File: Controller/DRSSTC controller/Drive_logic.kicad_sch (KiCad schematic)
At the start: 70 parts, among them J501 Conn_01x01_Female, J502 Screw_Terminal_01x02, J503 Conn_01x01_Female, J504 Conn_01x01_Female, J505 Screw_Terminal_01x02, J506 Conn_01x01_Female, J507 Conn_01x03_Male, J508 Conn_01x02_Male, J509 Conn_01x02_Male, J510 Conn_01x02_Male, U501 Optical_reciver, U502 Optical_reciver, U503 74HC14, U504 LM311, U505 74HC74, U506 74LS00, U507 TLV7031DBV

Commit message: 0.1V control-circuit
Next relese:
Mounting holes;
Fan header;
Better layout;
Bigger  capacitors;
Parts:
- removed J501, J503, J504, J506: Conn_01x01_Female, Connector_PinHeader_2.54mm:PinHeader_1x01_P2.54mm_Vertical, symbol Connector:Conn_01x01_Female
- removed J502, J505: Screw_Terminal_01x02, TerminalBlock:TerminalBlock_Altech_AK300-2_P5.00mm, symbol Connector:Screw_Terminal_01x02
- added J1, J3, J4, J6: Conn_01x01_Female, Connector_PinHeader_2.54mm:PinHeader_1x01_P2.54mm_Vertical, symbol Connector:Conn_01x01_Female
- added J2, J5: Screw_Terminal_01x02, TerminalBlock_Phoenix:TerminalBlock_Phoenix_PT-1,5-2-3.5-H_1x02_P3.50mm_Horizontal, symbol Connector:Screw_Terminal_01x02
- C513: footprint Capacitor_SMD:C_01005_0402Metric -> Capacitor_SMD:C_0805_2012Metric
- D509, D510: footprint (none) -> LED_SMD:LED_0805_2012Metric
- R503: footprint Resistor_SMD:R_0805_2012Metric -> Resistor_SMD:R_2010_5025Metric
- R506: footprint Resistor_SMD:R_1206_3216Metric -> Resistor_SMD:R_2010_5025Metric
- R515, R516: footprint (none) -> Resistor_SMD:R_0805_2012Metric
- RV501: value 19k -> 10k
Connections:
- net at C509.2, R505.2: now also J5.1 (Pin_1), J6.1 (Pin_1)
- net at C509.1, C511.1, J507.2 (Pin_2)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: now also J4.1 (Pin_1), J5.2 (Pin_2)
- net at D503.2 (A), D504.1 (K): now also J2.1 (Pin_1), J3.1 (Pin_1)
- net at D501.2 (A), D502.1 (K): now also J1.1 (Pin_1), J2.2 (Pin_2)

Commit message: V0.2a
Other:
- company: (none) -> Politehnika
- title: (none) -> DRSSTC controller
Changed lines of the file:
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@@
 (kicad_sch (version 20211123) (generator eeschema)
   (paper "A4")
+  (title_block
+    (title "DRSSTC controller")
+    (date "2023-03-07")
+    (rev "0.2")
+    (company "Politehnika")
+  )
   (junction (at 73.025 24.765) (diameter 0) (color 0 0 0 0)
   )

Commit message: V0.2c
Added stl files
PCB update
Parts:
- renumbered C501 to C301, C502 to C302, C503 to C303, C504 to C304, C505 to C305, C506 to C306, C507 to C307, C508 to C308, C509 to C309, C510 to C310, C511 to C311, C512 to C312, C513 to C313, C514 to C314, C515 to C315, D501 to D301, D502 to D302, D503 to D303, D504 to D304, D505 to D305, D506 to D306, D507 to D307, D508 to D308, D509 to D309, D510 to D310, D511 to D311, J1 to J301, J2 to J302, J3 to J303, J4 to J304, J5 to J305, J6 to J306, J507 to J307, J508 to J308, J509 to J309, J510 to J310, L501 to L301, R501 to R301, R502 to R302, R503 to R303, R504 to R304, R505 to R305, R506 to R306, R507 to R307, R508 to R308, R509 to R309, R510 to R310, R511 to R311, R512 to R312, R513 to R313, R514 to R314, R515 to R315, R516 to R316, R517 to R317, R518 to R318, R519 to R319, RV501 to RV301, TP501 to TP301, TP502 to TP302, TP503 to TP303, TP504 to TP304, TP505 to TP305, TP506 to TP306, U501 to U301, U502 to U302, U503 to U303, U504 to U304, U505 to U305, U506 to U306, U507 to U307

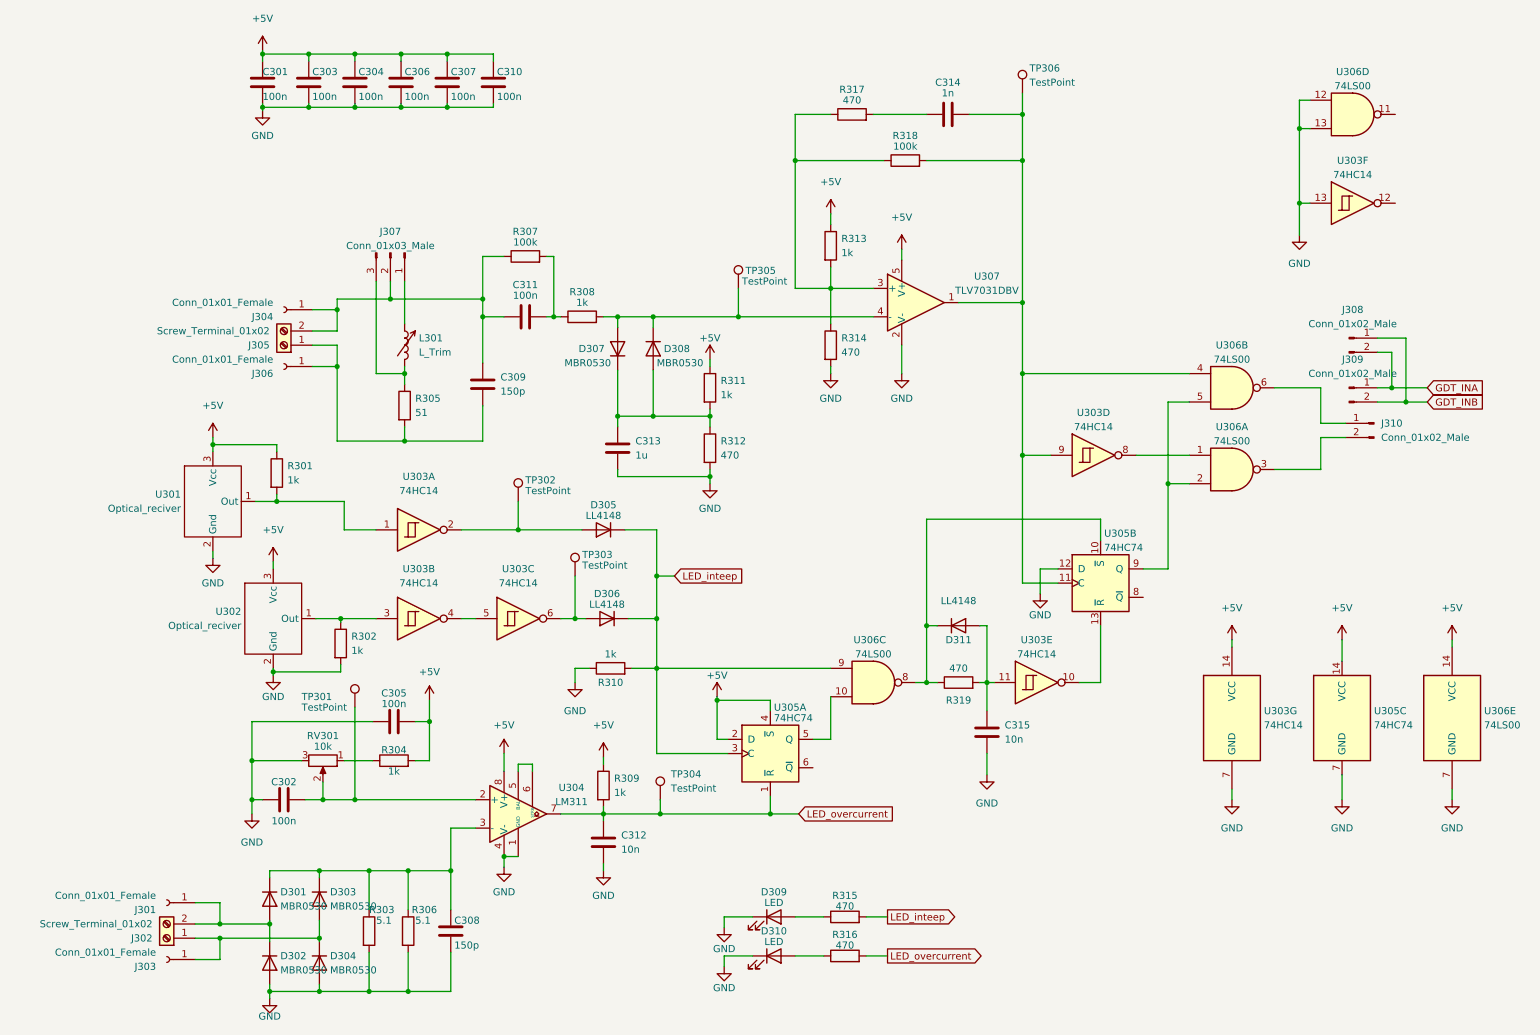
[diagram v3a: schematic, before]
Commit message: Updated circuit
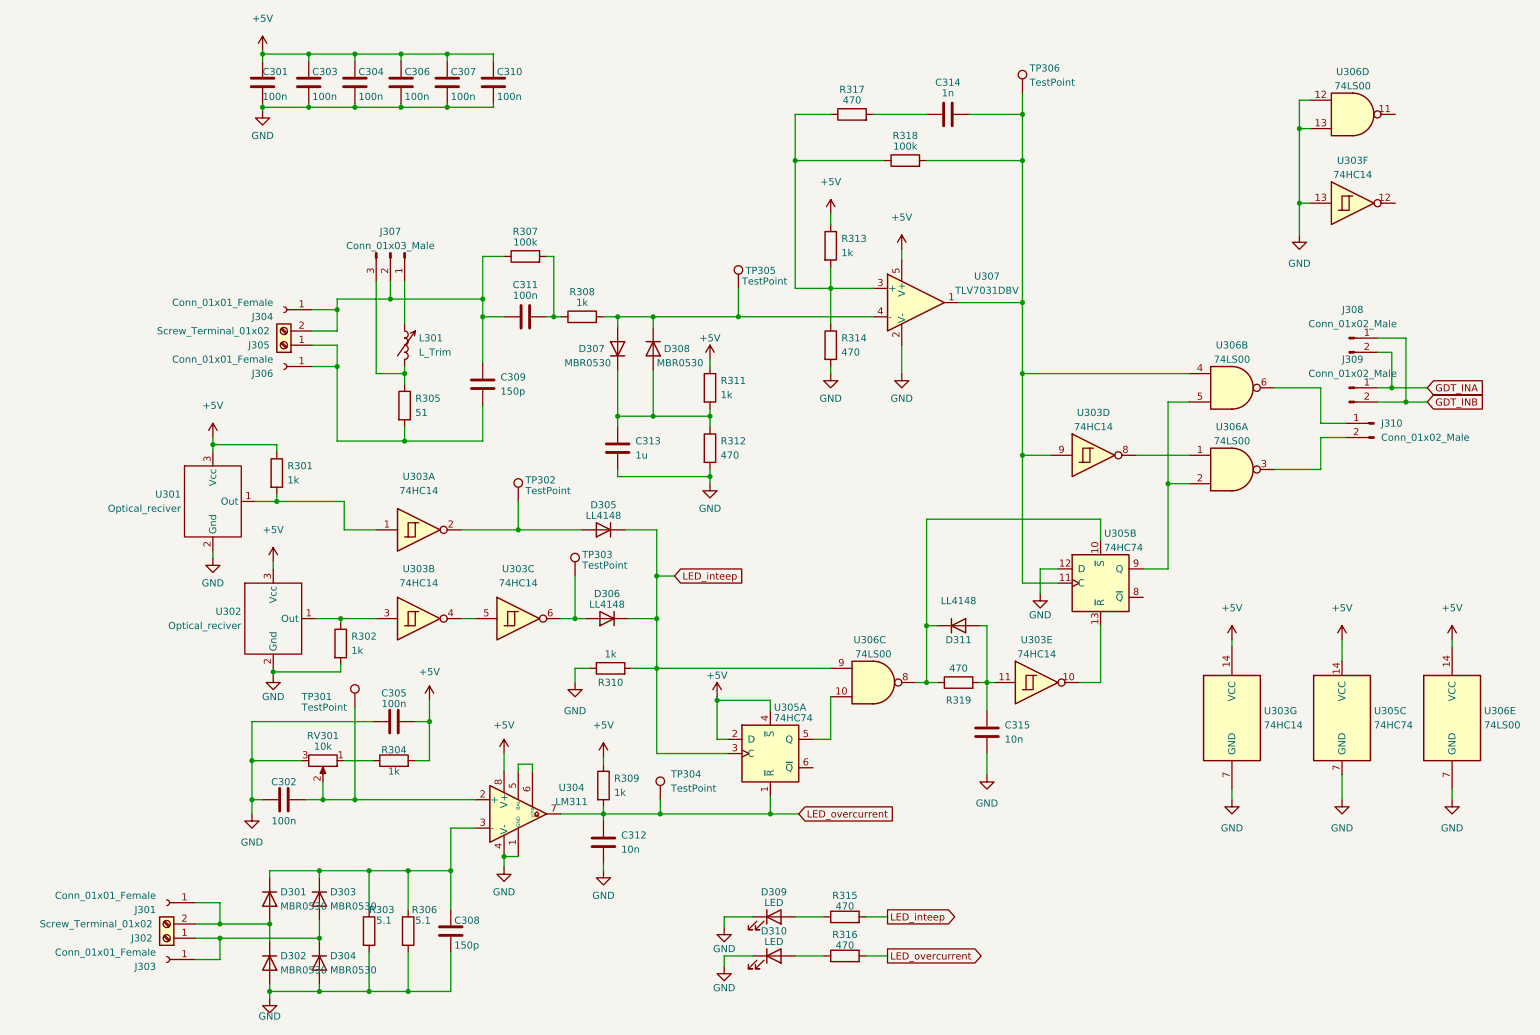
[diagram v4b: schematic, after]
